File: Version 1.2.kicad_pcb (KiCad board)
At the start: 4 copper layers, 40 x 40 mm, 33 parts, among them J1 Conn_01x04_Pin, J2 Screw_Terminal_01x02, J3 Conn_01x07_Pin, J4 Conn_Coaxial, U1 BGA2801, U2 BGA420, U3 AS179-92LF, U4 SX1278, U5 74LVC1G19, Y1 ECS-TXO-2520-33-400-AN-TR

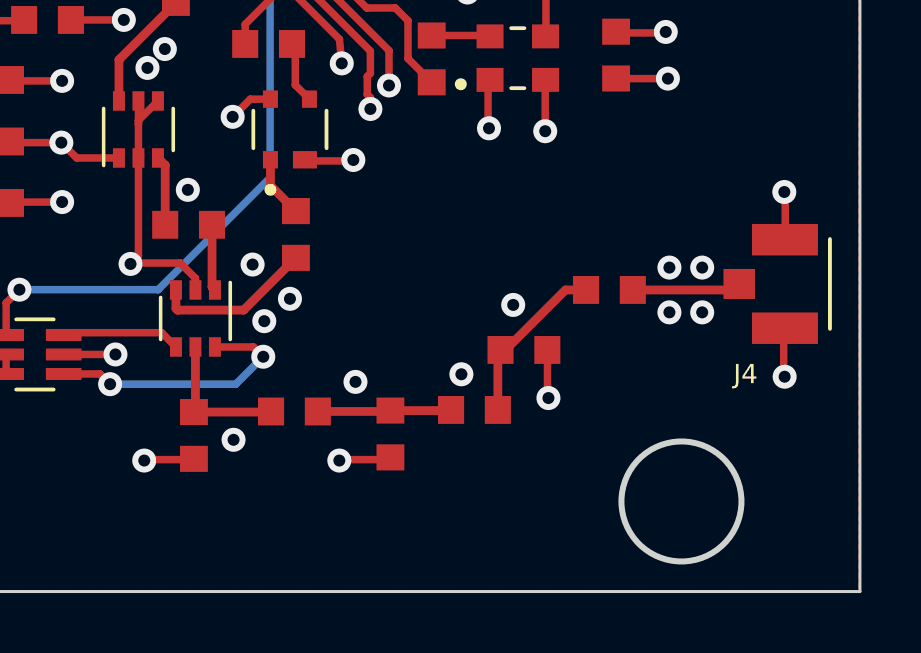
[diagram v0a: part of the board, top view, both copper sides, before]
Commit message: Fixed RF Line. Made Components closer together to improve impedance matching, straightened RF Path to reduce electron collision.
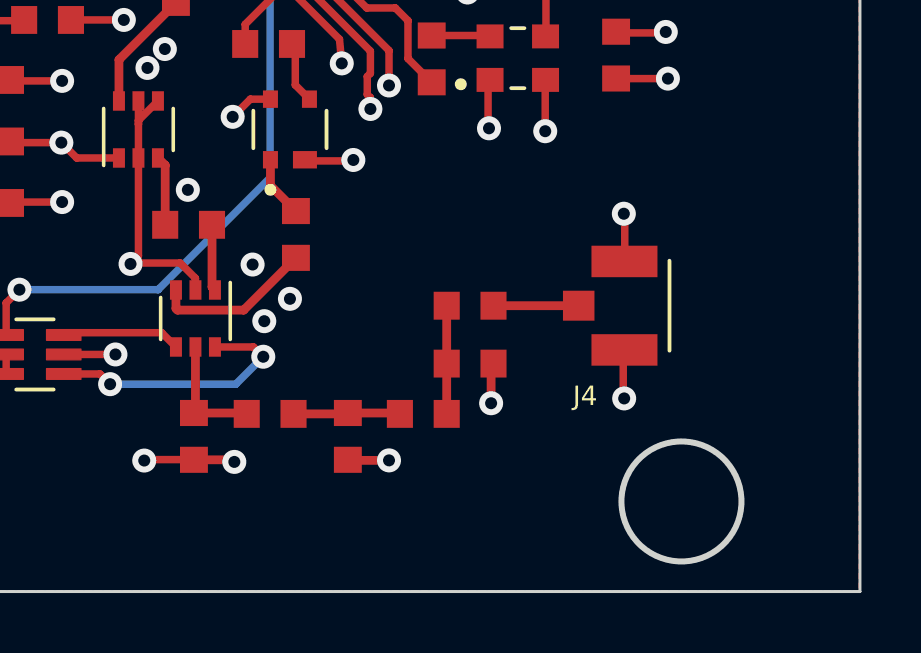
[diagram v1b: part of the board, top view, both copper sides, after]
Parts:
- moved J4 5.40 mm to (148.7, 99.8)
- moved L3 4.67 mm to (143.5, 99.8)
- moved C5 1.85 mm to (143.5, 101.7)
- moved L2 1.71 mm to (142.0, 103.4)
- moved C4 1.42 mm to (139.4, 104.1)
- moved L1 0.81 mm to (136.9, 103.4)
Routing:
- net Net-(C5-Pad1): track 5.72 -> 3.61 mm
- net Net-(C4-Pad1): track 4.46 -> 3.57 mm
- net /Filter_Input: track 4.77 -> 3.96 mm
- net /Filter_Output: track 3.63 -> 2.84 mm
- net GND: track 76.0 -> 76.6 mm, vias 39 -> 32
